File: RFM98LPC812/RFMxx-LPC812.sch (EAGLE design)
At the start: 14 parts, among them X1 BU-SMA-V, X2 BU-SMA-V

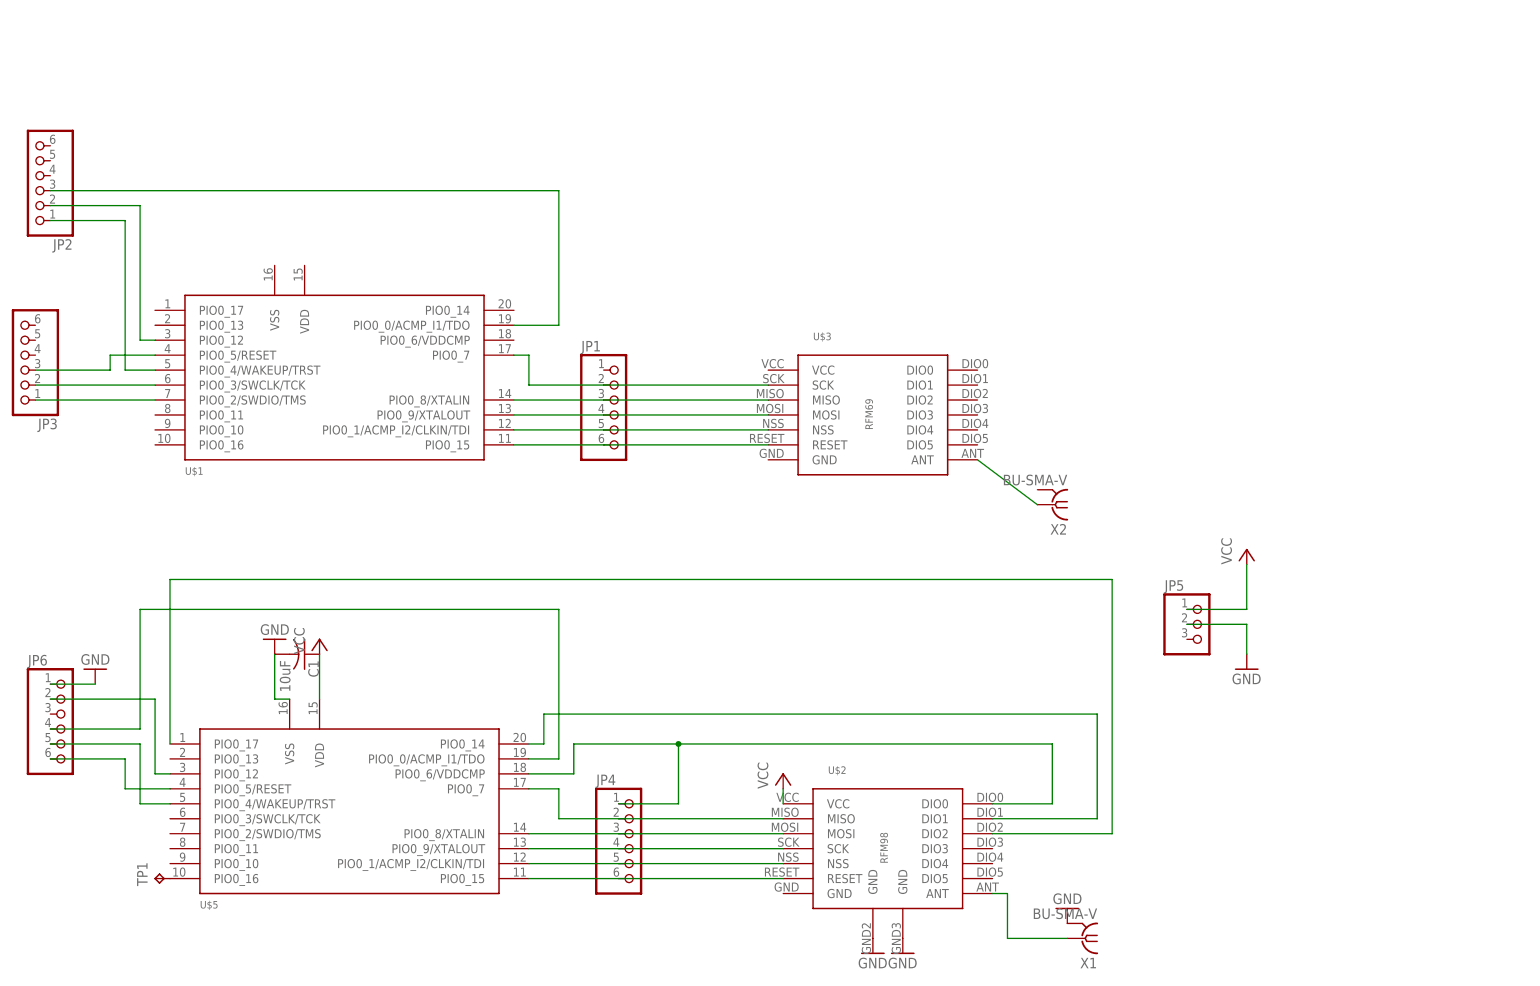
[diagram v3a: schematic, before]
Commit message: start working on RFM69
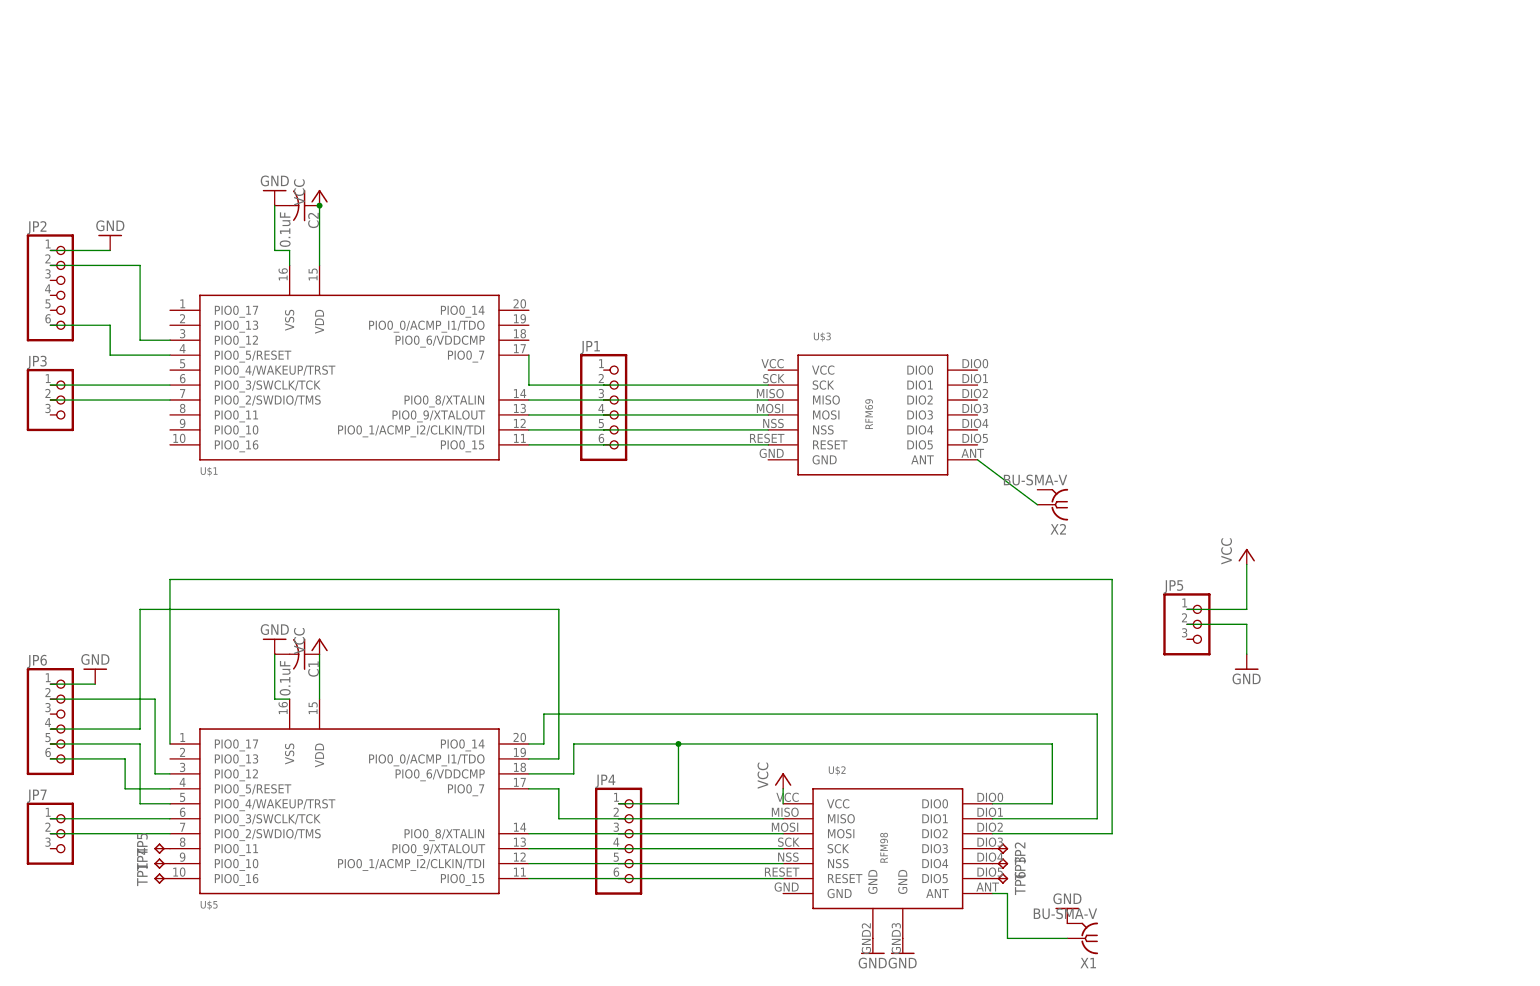
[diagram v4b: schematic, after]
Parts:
- added C2: 0.1uF, adafruit:C-USC0805
- added JP7: (no value), adafruit:PINHD-1X3
- added TP2, TP3, TP4, TP5, TP6: TPB1,27, testpad:TPB1,27
- C1: value 10uF -> 0.1uF
- JP3: device adafruit:PINHD-1X6 -> adafruit:PINHD-1X3
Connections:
- removed net N$2: JP3.1, U$1.PIO0_2/SWDIO/TMS
- removed net N$24: JP2.3, U$1.PIO0_0/ACMP_I1/TDO
- removed net N$4 (its old number): JP3.3, U$1.PIO0_5/RESET
- new net N$23: JP3.2, U$1.PIO0_2/SWDIO/TMS
- new net N$28: JP7.1, U$5.PIO0_3/SWCLK/TCK
- new net N$29: JP7.2, U$5.PIO0_2/SWDIO/TMS
- new net N$30: TP2.TP, U$2.DIO3
- new net N$31: TP3.TP, U$2.DIO4
- new net N$32: TP4.TP, U$5.PIO0_10
- new net N$33: TP5.TP, U$5.PIO0_11
- new net N$34: TP6.TP, U$2.DIO5
- net GND: now also C2.2, JP2.1, U$1.VSS
- net N$3: now also JP3.1; no longer JP3.2
- net N$5: now also JP2.6, U$1.PIO0_5/RESET; no longer JP2.1, U$1.PIO0_4/WAKEUP/TRST
- net VCC: now also C2.1, U$1.VDD
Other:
- moved on the sheet: JP2, U$1

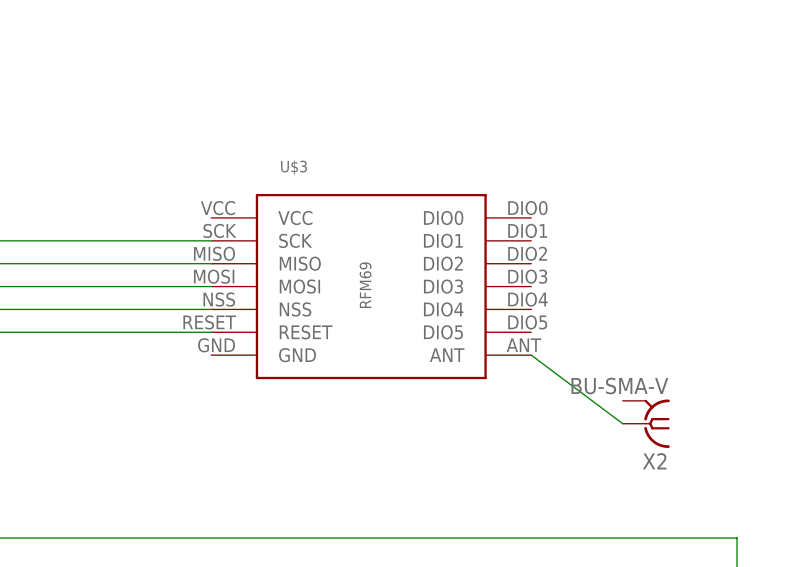
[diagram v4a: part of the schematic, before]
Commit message: start removing ground plane on RFM98 side
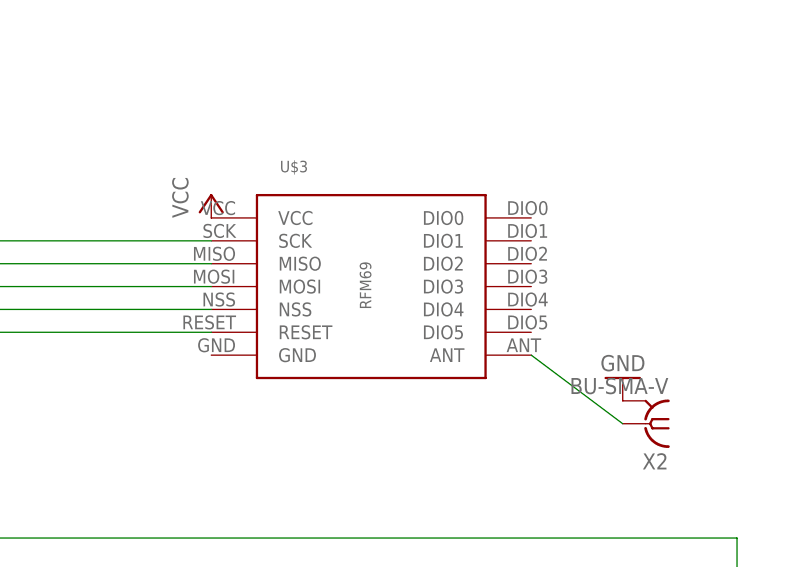
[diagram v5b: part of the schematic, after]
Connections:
- net GND: now also X2.2
- net VCC: now also U$3.VCC
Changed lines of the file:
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@@
 <part name="P+2" library="supply1" deviceset="VCC" device=""/>
 <part name="JP3" library="adafruit" deviceset="PINHD-1X3" device=""/>
+<part name="GND_RFM4" library="supply1" deviceset="GND" device=""/>
+<part name="P+5" library="supply1" deviceset="VCC" device=""/>
 </parts>
 <sheets>
@@
 <instance part="P+2" gate="VCC" x="-93.98" y="78.74"/>
 <instance part="JP3" gate="A" x="-137.16" y="43.18"/>
+<instance part="GND_RFM4" gate="1" x="27.94" y="30.48" rot="R180"/>
+<instance part="P+5" gate="VCC" x="-17.78" y="50.8"/>
 </instances>
 <busses>
@@
 <pinref part="P+2" gate="VCC" pin="VCC"/>
 <junction x="-93.98" y="76.2"/>
+</segment>
+<segment>
+<pinref part="U$3" gate="G$1" pin="VCC"/>
+<pinref part="P+5" gate="VCC" pin="VCC"/>
 </segment>
 </net>
@@
 <wire x1="-101.6" y1="68.58" x2="-101.6" y2="76.2" width="0.1524" layer="91"/>
 </segment>
-</net>
+<segment>
+<pinref part="X2" gate="G$1" pin="2"/>
+<pinref part="GND_RFM4" gate="1" pin="GND"/>
+</segment>
+</net>
